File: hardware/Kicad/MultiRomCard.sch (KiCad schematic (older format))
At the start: 18 parts, among them P1 VC4000_Cartridge_Bus, P2 MicroSD_Breakout, P3 Test Header, U1 Arduino_Nano, U2 74HC595, U3 74HC595, U4 74HC595, U5 6264, U6 74HC245, U7 74HC245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

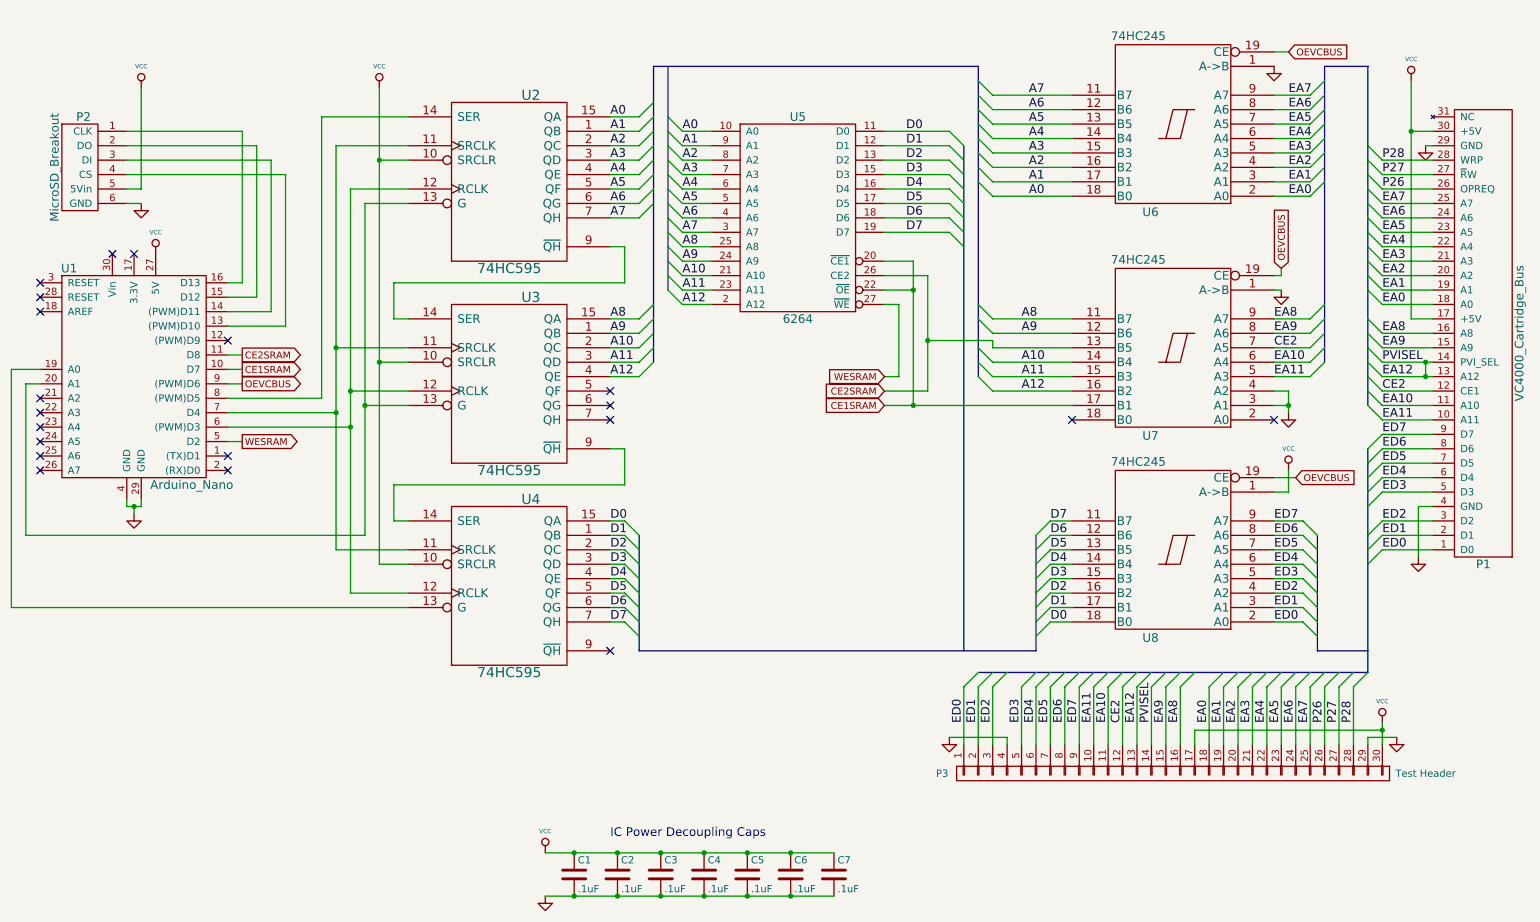
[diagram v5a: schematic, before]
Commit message: [SCH/PCB] Correct 74HC245 direction pins.
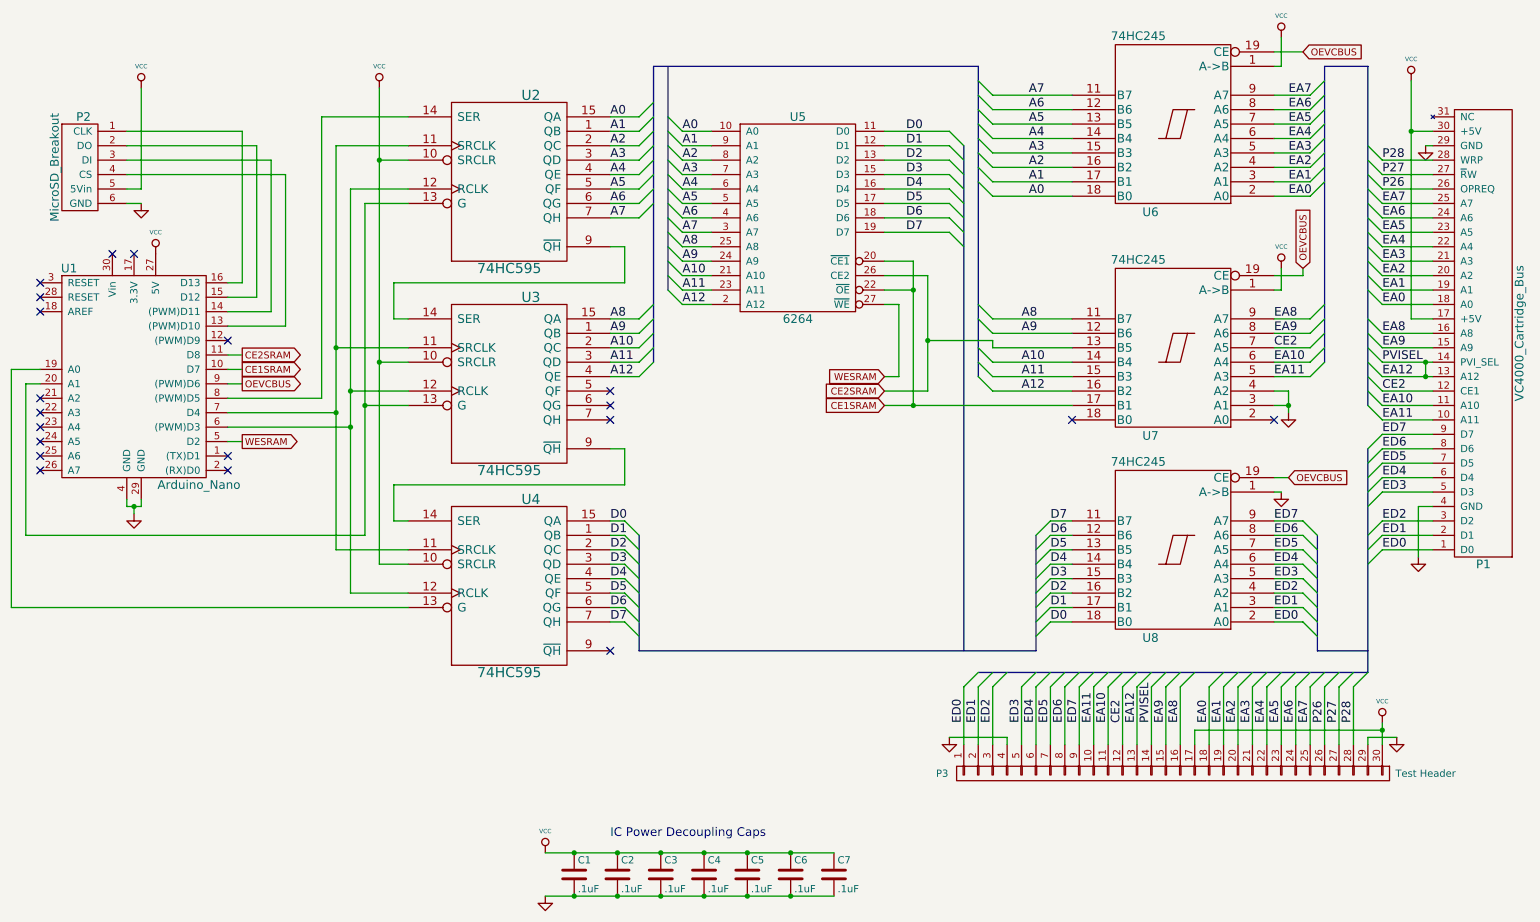
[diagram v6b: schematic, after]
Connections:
- net GND: now also U8.1 (A->B); no longer U6.1 (A->B), U7.1 (A->B)
- net VCC: now also U6.1 (A->B), U7.1 (A->B); no longer U8.1 (A->B)
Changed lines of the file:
@@
 LIBS:valves
 LIBS:MultiRomCard
-LIBS:MultiRomCard-cache
 EELAYER 25 0
 EELAYER END
@@
 Sheet 1 1
 Title "Interton VC4000 MultiRom Cartridge"
-Date "Thursday, June 25, 2015"
+Date "Monday, June 29, 2015"
 Rev "0.1"
 Comp "Mario Keller and Johannes Maibaum"
@@
 	1    4150 5100
 	1    0    0    -1
-$EndComp
-$Comp
-L 74HC245 U6
-U 1 1 54D634ED
-P 8750 1900
-F 0 "U6" H 8850 2475 60  0000 L BNN
-F 1 "74HC245" H 8800 1325 60  0000 L TNN
-F 2 "Housings_DIP:DIP-20__300_ELL" H 8750 1900 60  0001 C CNN
-F 3 "" H 8750 1900 60  0000 C CNN
-	1    8750 1900
-	-1   0    0    1
 $EndComp
 $Comp
@@
 L GND #PWR04
 U 1 1 54DB55F6
-P 9500 3050
-F 0 "#PWR04" H 9500 3050 30  0001 C CNN
-F 1 "GND" H 9500 2980 30  0001 C CNN
-F 2 "" H 9500 3050 60  0000 C CNN
-F 3 "" H 9500 3050 60  0000 C CNN
-	1    9500 3050
+P 9500 4450
+F 0 "#PWR04" H 9500 4450 30  0001 C CNN
+F 1 "GND" H 9500 4380 30  0001 C CNN
+F 2 "" H 9500 4450 60  0000 C CNN
+F 3 "" H 9500 4450 60  0000 C CNN
+	1    9500 4450
 	1    0    0    -1
 $EndComp
@@
 L VCC #PWR05
 U 1 1 54DB5800
-P 9550 4300
-F 0 "#PWR05" H 9550 4400 30  0001 C CNN
-F 1 "VCC" H 9550 4450 30  0000 C CNN
-F 2 "" H 9550 4300 60  0000 C CNN
-F 3 "" H 9550 4300 60  0000 C CNN
-	1    9550 4300
+P 9500 2900
+F 0 "#PWR05" H 9500 3000 30  0001 C CNN
+F 1 "VCC" H 9500 3050 30  0000 C CNN
+F 2 "" H 9500 2900 60  0000 C CNN
+F 3 "" H 9500 2900 60  0000 C CNN
+	1    9500 2900
 	1    0    0    -1
 $EndComp
 Text GLabel 2300 3700 2    48   Output ~ 0
 OEVCBUS
-Text GLabel 9500 2900 1    48   Input ~ 0
+Text GLabel 9650 2900 1    48   Input ~ 0
 OEVCBUS
-Text GLabel 9600 4350 2    48   Input ~ 0
+Text GLabel 9550 4350 2    48   Input ~ 0
 OEVCBUS
-Text GLabel 9550 1400 2    48   Input ~ 0
+Text GLabel 9650 1400 2    48   Input ~ 0
 OEVCBUS
 NoConn ~ 9450 3950
@@
 $Comp
 L GND #PWR010
-U 1 1 5587E073
-P 9450 1500
-F 0 "#PWR010" H 9450 1500 30  0001 C CNN
-F 1 "GND" H 9450 1430 30  0001 C CNN
-F 2 "" H 9450 1500 60  0000 C CNN
-F 3 "" H 9450 1500 60  0000 C CNN
-	1    9450 1500
-	1    0    0    -1
-$EndComp
-$Comp
-L GND #PWR011
 U 1 1 5587E24F
 P 10500 2050
-F 0 "#PWR011" H 10500 2050 30  0001 C CNN
+F 0 "#PWR010" H 10500 2050 30  0001 C CNN
 F 1 "GND" H 10500 1980 30  0001 C CNN
 F 2 "" H 10500 2050 60  0000 C CNN
@@
 $EndComp
 $Comp
-L GND #PWR012
+L GND #PWR011
 U 1 1 5587EA58
 P 1600 2450
-F 0 "#PWR012" H 1600 2450 30  0001 C CNN
+F 0 "#PWR011" H 1600 2450 30  0001 C CNN
 F 1 "GND" H 1600 2380 30  0001 C CNN
 F 2 "" H 1600 2450 60  0000 C CNN
@@
 Connection ~ 10400 1950
 Wire Wire Line
-	9550 1400 9450 1400
-Wire Wire Line
-	9600 4350 9450 4350
-Wire Wire Line
-	9550 4300 9550 4450
-Wire Wire Line
-	9550 4450 9450 4450
+	9650 1400 9450 1400
+Wire Wire Line
+	9550 4350 9450 4350
+Wire Wire Line
+	9500 4450 9450 4450
 Wire Bus Line
 	10100 5700 10100 4150
 Wire Wire Line
-	9500 2950 9450 2950
-Wire Wire Line
-	9500 2950 9500 2900
+	9650 2950 9450 2950
+Wire Wire Line
+	9650 2950 9650 2900
 Wire Wire Line
 	9450 3050 9500 3050
@@
 	1500 2450 1600 2450
 $Comp
-L VCC #PWR013
+L VCC #PWR012
 U 1 1 5587FD9D
 P 1600 1650
-F 0 "#PWR013" H 1600 1750 30  0001 C CNN
+F 0 "#PWR012" H 1600 1750 30  0001 C CNN
 F 1 "VCC" H 1600 1800 30  0000 C CNN
 F 2 "" H 1600 1650 60  0000 C CNN
@@
 	-1   0    0    -1
 $EndComp
-$Comp
-L Arduino_Nano U1
-U 1 1 558812C5
-P 1550 3650
-F 0 "U1" H 1100 4400 60  0000 C CNN
-F 1 "Arduino_Nano" H 1950 2900 60  0000 C CNN
-F 2 "VC4000_MultiRom:Arduino_Nano" H 1550 3500 60  0001 C CNN
-F 3 "" H 1550 3500 60  0000 C CNN
-	1    1550 3650
-	1    0    0    -1
-$EndComp
 Wire Wire Line
 	800  3700 900  3700
@@
 NoConn ~ 900  3900
 $Comp
-L GND #PWR014
+L GND #PWR013
 U 1 1 54D739DD
 P 1550 4600
-F 0 "#PWR014" H 1550 4600 30  0001 C CNN
+F 0 "#PWR013" H 1550 4600 30  0001 C CNN
 F 1 "GND" H 1550 4530 30  0001 C CNN
 F 2 "" H 1550 4600 60  0000 C CNN
@@
 	7600 6150 7200 6150
 $Comp
-L GND #PWR015
+L GND #PWR014
 U 1 1 558C6EB1
 P 7200 6150
-F 0 "#PWR015" H 7200 6150 30  0001 C CNN
+F 0 "#PWR014" H 7200 6150 30  0001 C CNN
 F 1 "GND" H 7200 6080 30  0001 C CNN
 F 2 "" H 7200 6150 60  0000 C CNN
@@
 	10100 6200 10100 6150
 $Comp
-L GND #PWR016
+L GND #PWR015
 U 1 1 558C7DE5
 P 10300 6150
-F 0 "#PWR016" H 10300 6150 30  0001 C CNN
+F 0 "#PWR015" H 10300 6150 30  0001 C CNN
 F 1 "GND" H 10300 6080 30  0001 C CNN
 F 2 "" H 10300 6150 60  0000 C CNN
@@
 	10100 6150 10300 6150
 $Comp
-L VCC #PWR017
+L VCC #PWR016
 U 1 1 558C7FFB
 P 10200 6050
-F 0 "#PWR017" H 10200 6150 30  0001 C CNN
+F 0 "#PWR016" H 10200 6150 30  0001 C CNN
 F 1 "VCC" H 10200 6200 30  0000 C CNN
 F 2 "" H 10200 6050 60  0000 C CNN
@@
 Text Label 10000 6050 1    60   ~ 0
 P28
+Wire Wire Line
+	9500 3050 9500 2900
+$Comp
+L 74HC245 U6
+U 1 1 54D634ED
+P 8750 1900
+F 0 "U6" H 8850 2475 60  0000 L BNN
+F 1 "74HC245" H 8800 1325 60  0000 L TNN
+F 2 "Housings_DIP:DIP-20__300_ELL" H 8750 1900 60  0001 C CNN
+F 3 "" H 8750 1900 60  0000 C CNN
+	1    8750 1900
+	-1   0    0    1
+$EndComp
+Wire Wire Line
+	9450 1500 9500 1500
+Wire Wire Line
+	9500 1500 9500 1300
+$Comp
+L VCC #PWR017
+U 1 1 559131AE
+P 9500 1300
+F 0 "#PWR017" H 9500 1400 30  0001 C CNN
+F 1 "VCC" H 9500 1450 30  0000 C CNN
+F 2 "" H 9500 1300 60  0000 C CNN
+F 3 "" H 9500 1300 60  0000 C CNN
+	1    9500 1300
+	1    0    0    -1
+$EndComp
+$Comp
+L Arduino_Nano U1
+U 1 1 559141A6
+P 1550 3650
+F 0 "U1" H 1100 4400 60  0000 C CNN
+F 1 "Arduino_Nano" H 2000 2900 60  0000 C CNN
+F 2 "VC4000_MultiRom:Arduino_Nano" H 1550 3500 60  0001 C CNN
+F 3 "" H 1550 3500 60  0000 C CNN
+	1    1550 3650
+	1    0    0    -1
+$EndComp
 $EndSCHEMATC

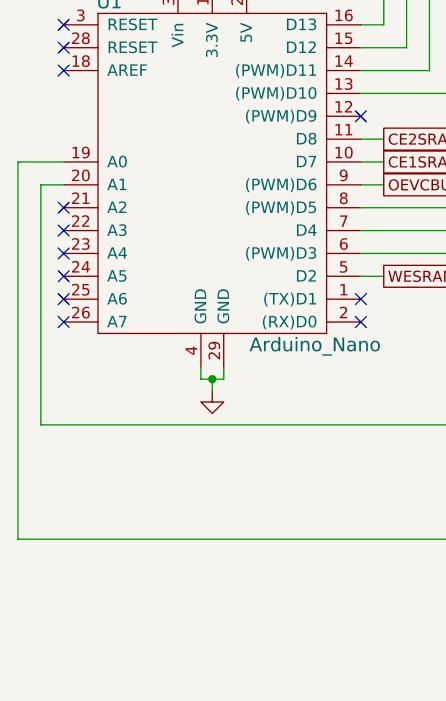
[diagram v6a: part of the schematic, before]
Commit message: [SCH/PCB] Corrected wrong analog pin numbering in Arduino Nano symbol.
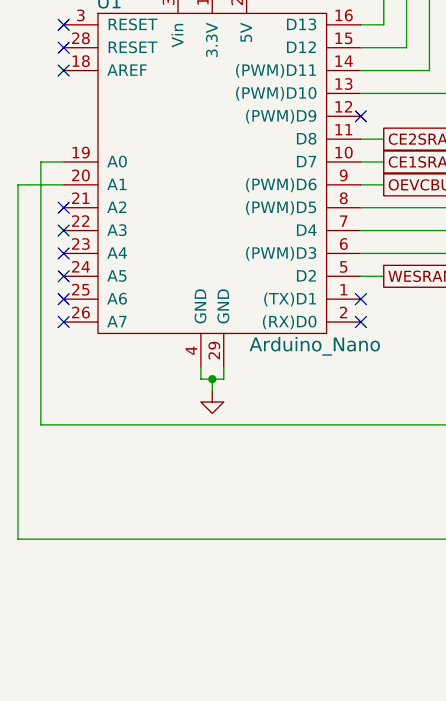
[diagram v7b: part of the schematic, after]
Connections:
- net at U2.13 (G), U3.13 (G): now also U1.19 (A0); no longer U1.20 (A1)
- net at U4.13 (G): now also U1.20 (A1); no longer U1.19 (A0)
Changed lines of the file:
@@
 LIBS:valves
 LIBS:MultiRomCard
+LIBS:MultiRomCard-cache
 EELAYER 25 0
 EELAYER END
@@
 Sheet 1 1
 Title "Interton VC4000 MultiRom Cartridge"
-Date "Monday, June 29, 2015"
+Date "Tuesday, July 21, 2015"
 Rev "0.1"
 Comp "Mario Keller and Johannes Maibaum"
@@
 	2850 1850 3450 1850
 Wire Wire Line
-	700  3600 700  5250
+	700  3700 700  5250
 Wire Wire Line
 	700  5250 3450 5250
@@
 Connection ~ 3150 3850
 Wire Wire Line
-	800  4750 800  3700
+	800  4750 800  3600
 Wire Wire Line
 	2950 3900 2200 3900
@@
 	-1   0    0    -1
 $EndComp
-Wire Wire Line
-	800  3700 900  3700
-Wire Wire Line
-	700  3600 900  3600
 NoConn ~ 900  3800
 NoConn ~ 900  3900
@@
 $Comp
 L Arduino_Nano U1
-U 1 1 559141A6
+U 1 1 55AE1829
 P 1550 3650
 F 0 "U1" H 1100 4400 60  0000 C CNN
@@
 	1    0    0    -1
 $EndComp
+Wire Wire Line
+	800  3600 900  3600
+Wire Wire Line
+	700  3700 900  3700
 $EndSCHEMATC
